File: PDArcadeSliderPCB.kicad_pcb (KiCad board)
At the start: 2 copper layers, 100 x 63.6 mm, 28 parts, among them J1 Conn_01x01_Male, J2 Conn_01x06_Male, J6 Conn_01x01_Male, J7 Conn_01x01_Male, J8 Conn_01x01_Male, J9 Conn_01x01_Male, U1 testsensorg, U2 testsensorg, U3 testsensorg, U4 testsensorg, U5 testsensorg, U6 testsensorg

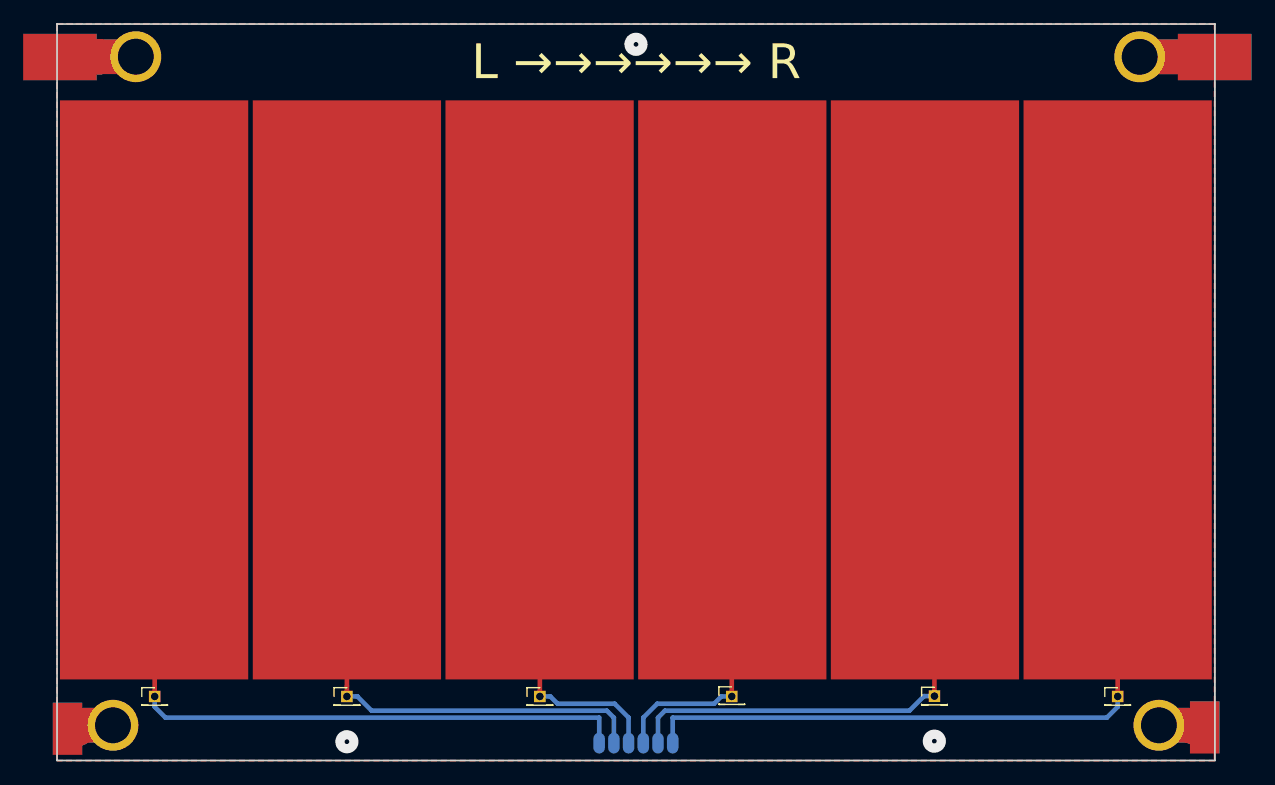
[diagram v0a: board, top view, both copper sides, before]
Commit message: Trying to find better hatching settings
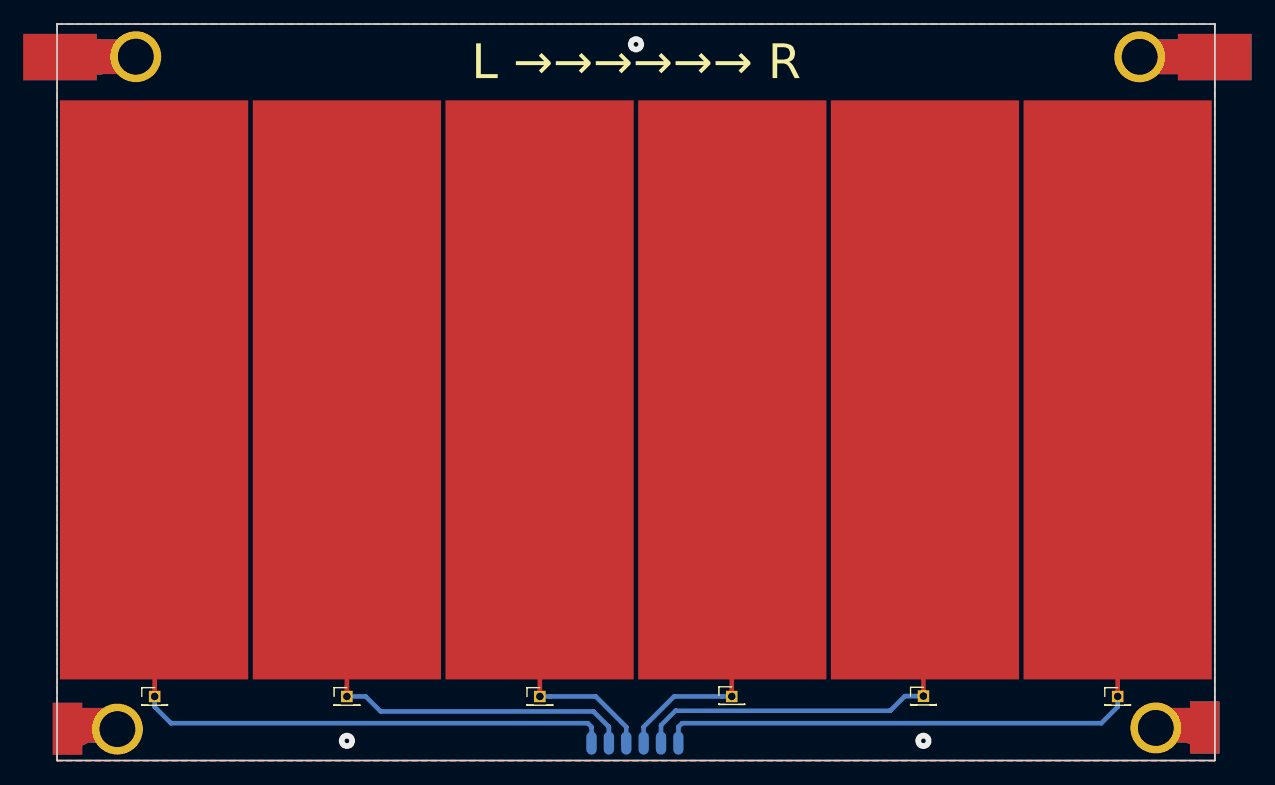
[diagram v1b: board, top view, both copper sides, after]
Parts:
- moved J6 0.95 mm to (174.9, 161.7)
- moved REF** 0.50 mm to (105.3, 166.2)
- moved REF** 0.35 mm to (195.0, 166.2)
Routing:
- net Net-(J2-Pad2): track 72.5 -> 70.1 mm
- net Net-(J2-Pad6): track 68.4 -> 67.2 mm
- net Net-(J1-Pad1): track 107.2 -> 106.3 mm
- net Net-(J2-Pad5): track 52.5 -> 51.6 mm

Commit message: Ground hatching from old manual
Ground hatching from old manual
https://forum.kicad.info/t/copper-pour-with-hatched-fill-instead-of-solid-fill/860/8
because for now KiCad cannot make hatching like this
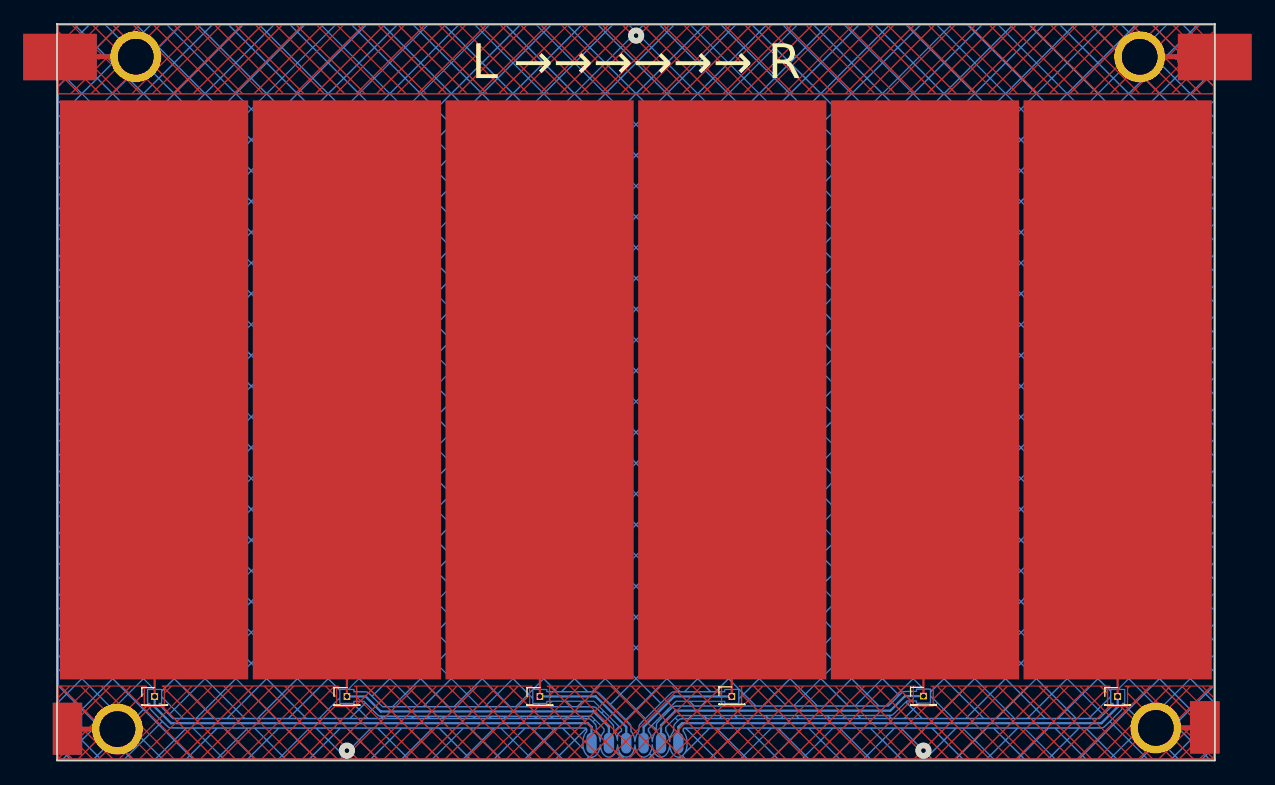
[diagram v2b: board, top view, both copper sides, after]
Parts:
- added G***: LOGO, LOGO, F.Cu at (150.1, 135.4)
- added J10: topgroundhatching, PDArcadeSliderPCB:TopHatching, F.Cu at (150.1, 135.4)
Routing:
- net GND: track 32.8 -> 42.1 mm
- removed copper zone on B.Cu, net GND
- removed copper zone on F.Cu, net GND
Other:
- rule pad_to_mask_clearance: 0.2 -> 0.1
- rule solder_mask_min_width: 0.25 -> 0.15
